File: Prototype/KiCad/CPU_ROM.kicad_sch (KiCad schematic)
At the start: 75 parts, among them J201 USB_B_Micro, J202 BOOT SEL, J203 Vic20 Cartridge Connector, J204 VGA, J205 SWD, J206 EDGE, J207 +5V, U201 TLV74311PDBVR, U202 W25Q16JVSSIQ, U203 RP2350B-QFN80, U204 74LVC1G06, U205 74LVC245A, U206 IS6xC1024AL-xxH, U207 6502 CPU, U208 74LVC245A, U209 LD1117S33TR_SOT223, U210 74LS245, U211 74CBTD3861, Y201 12MHz

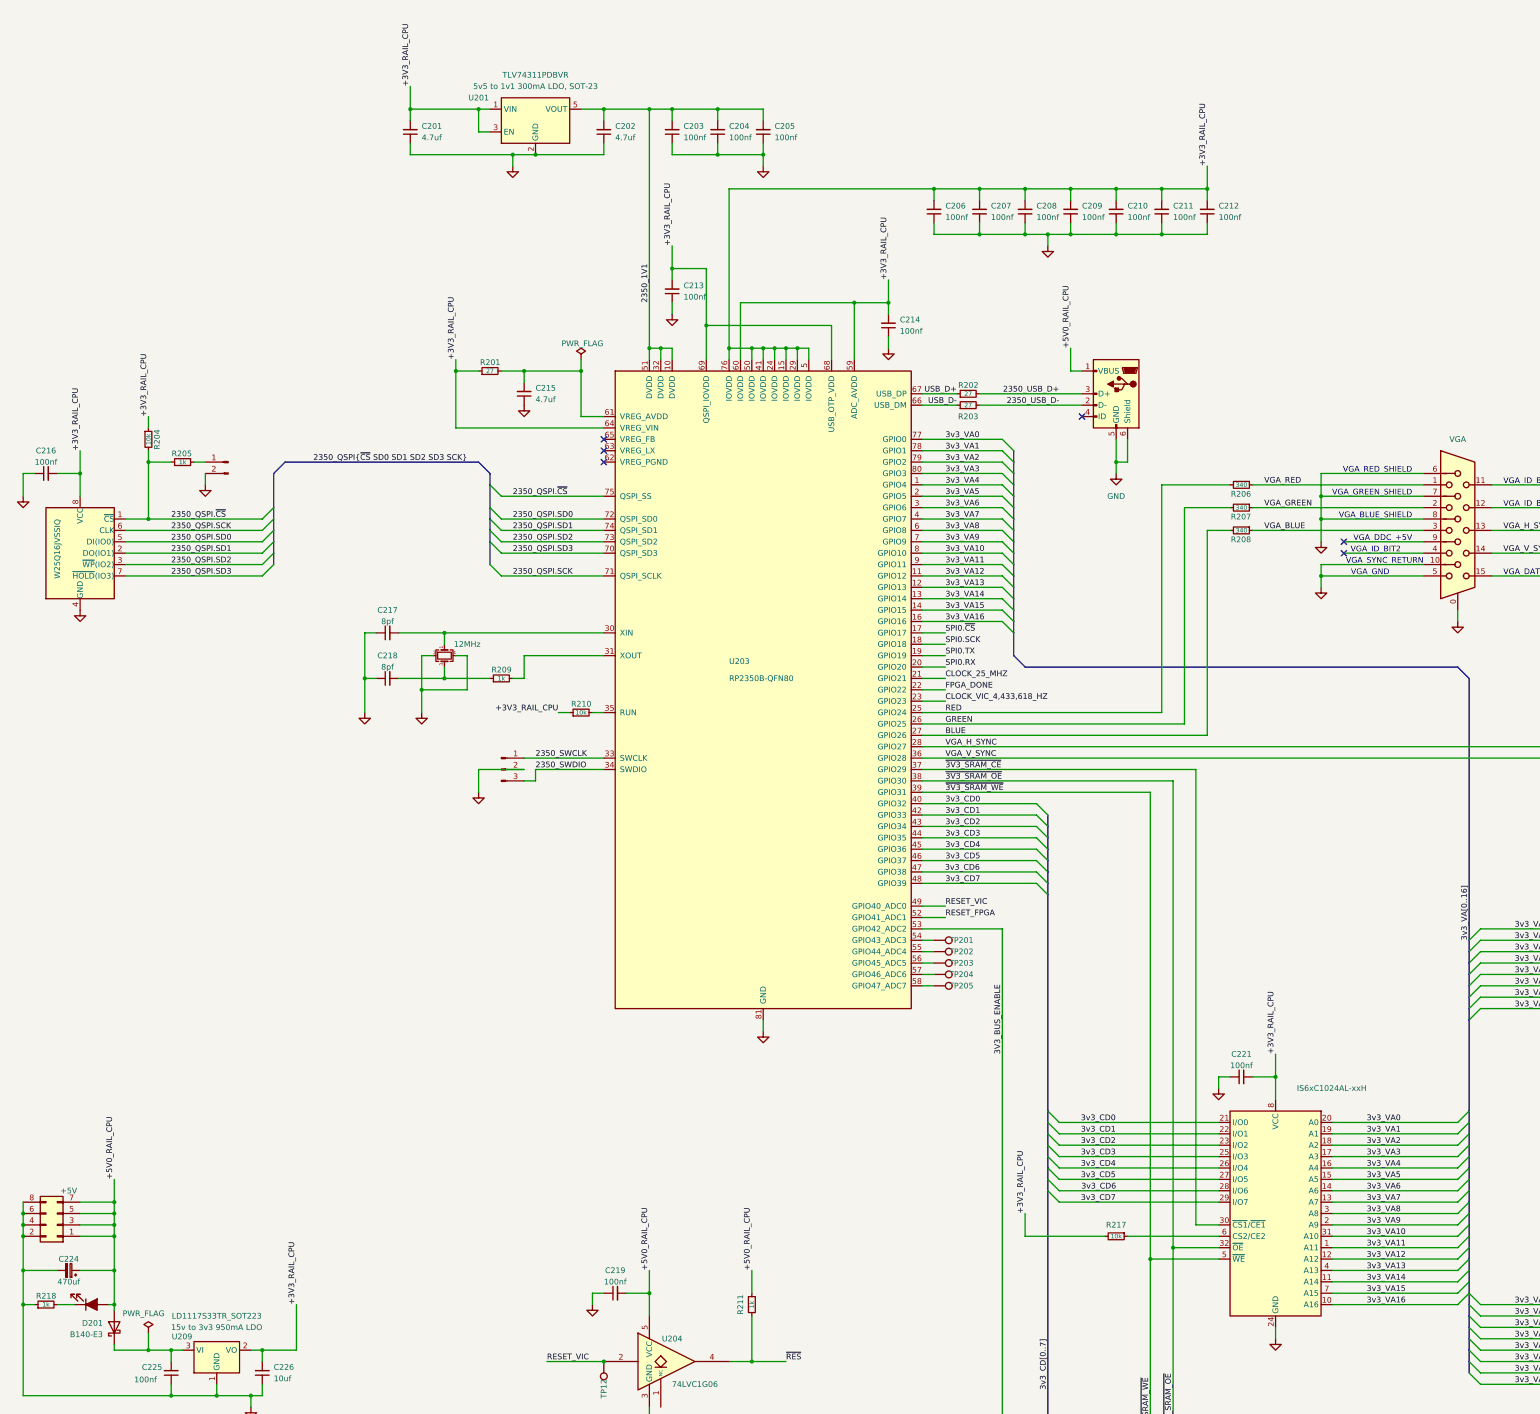
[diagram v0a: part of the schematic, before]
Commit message: - Updated to KiCad 10
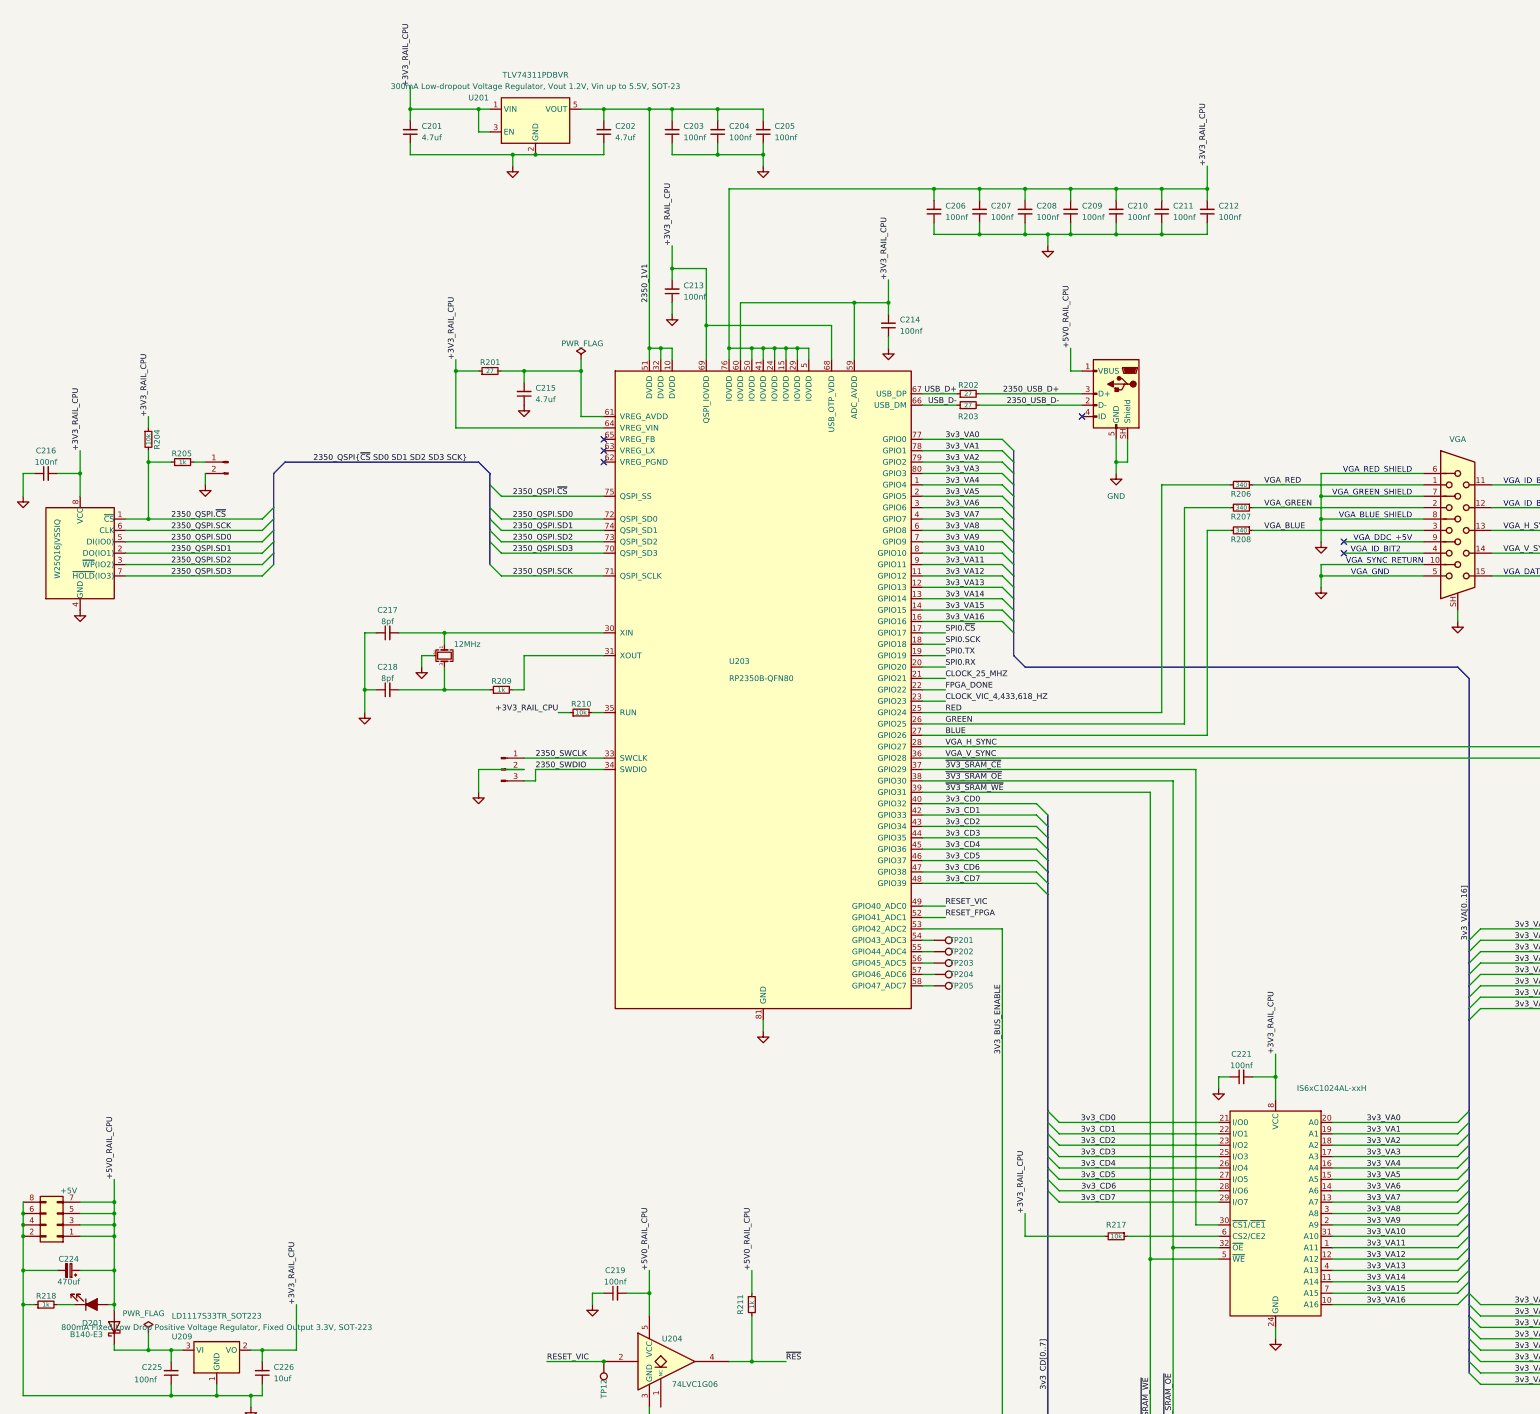
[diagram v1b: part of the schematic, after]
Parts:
- D201: footprint Diode_SMD:D_SOD-123 -> Diode_SMD:D_SMA
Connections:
- net GND: now also J201.SH (Shield), J204.SH; no longer J201.6 (Shield), J204.0
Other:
- moved on the sheet: C218, R209
